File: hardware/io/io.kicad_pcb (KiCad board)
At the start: 4 copper layers, 100 x 80 mm, 33 parts, among them P1 CONN_IO, P2 CONN_01X02, P3 CONN_USB, P4 CONN_01X08, U1 74LS125, U10 74LS173, U2 74LS32, U3 74LS173, U4 74LS00, U5 74LS173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

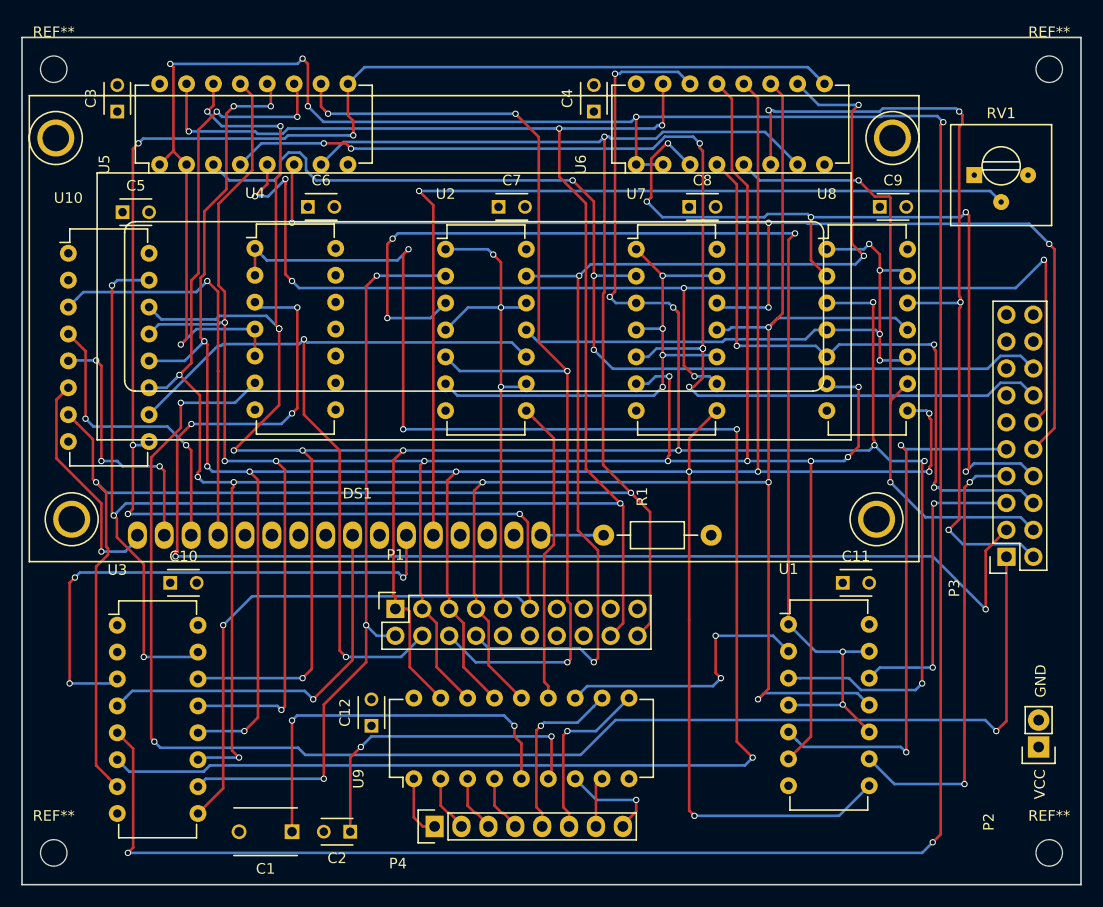
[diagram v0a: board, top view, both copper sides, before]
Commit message: Supply ~RST to USB interface
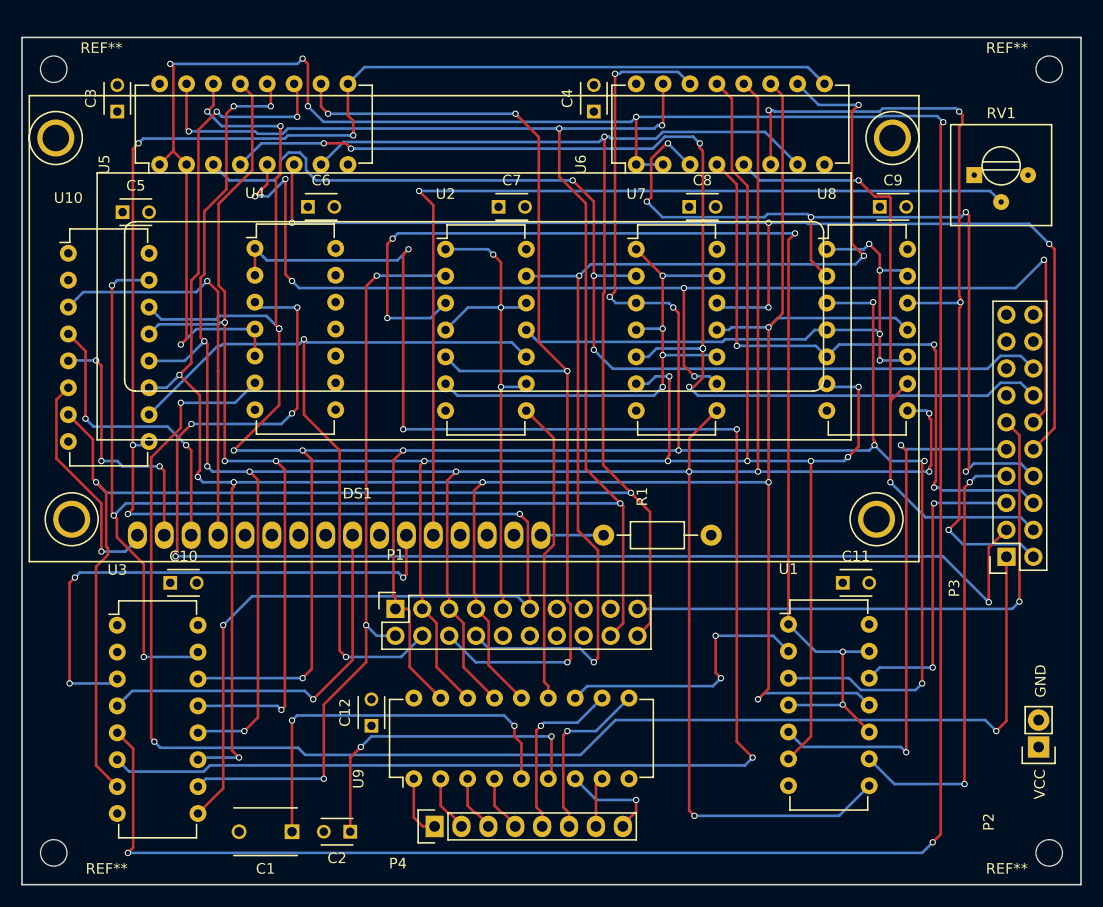
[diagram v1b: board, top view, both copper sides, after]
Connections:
- P1 pad 19: Net-(P1-Pad19) -> ~RST
- P3 pad 11: Net-(P3-Pad11) -> ~RST
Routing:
- net ~RST: track 0.00 -> 53.8 mm, vias 0 -> 1
- net ~USB_WR: track 124.3 -> 123.6 mm
